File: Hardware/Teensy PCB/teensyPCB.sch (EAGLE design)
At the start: 13 parts, among them U1 HC_05, U2 USD-SOCKETNEW

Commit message: Added wiring of the Linear Array sensor to the teency chip
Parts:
- added LINEAR_ARRAY_SENSOR2: (no value), SparkFun-Connectors:M05LOCK
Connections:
- removed net N$3: J2.1
- removed net N$4: J1.1
- new net AOUT: LINEAR_ARRAY_SENSOR2.1, U$1.16/A2/T
- new net CLK: LINEAR_ARRAY_SENSOR2.3, U$1.14/A0
- new net SI: LINEAR_ARRAY_SENSOR2.2, U$1.15/A1/T
- net 3.3V: now also LINEAR_ARRAY_SENSOR2.4
- net GND: now also LINEAR_ARRAY_SENSOR2.5
- net N$5: now also J1.1

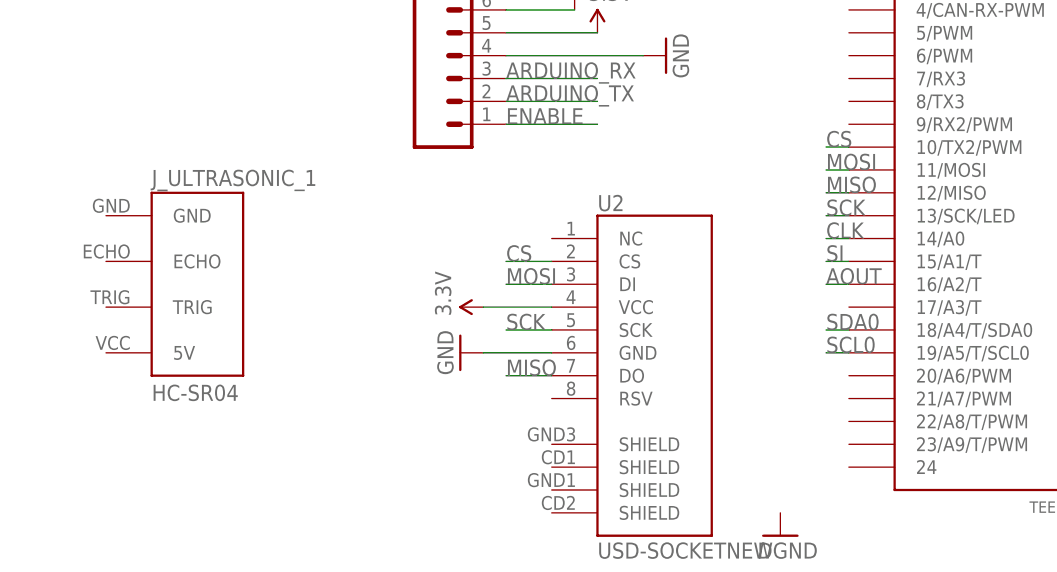
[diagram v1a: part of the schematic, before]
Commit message: Added the wiring for the ultrasonic sensor to the Teency chip
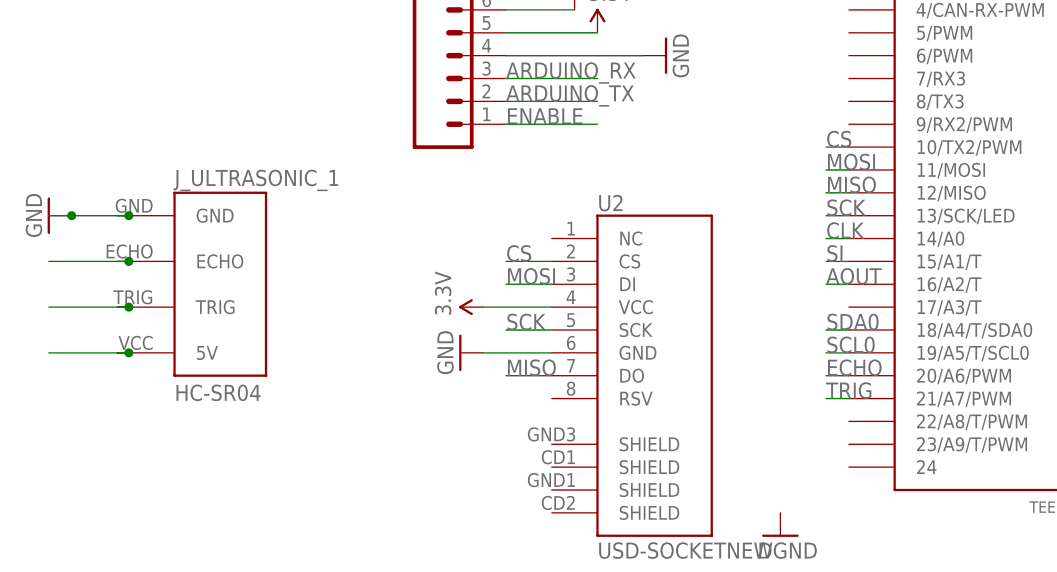
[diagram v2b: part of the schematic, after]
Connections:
- new net ECHO: J_ULTRASONIC_1.ECHO, U$1.20/A6/PWM
- new net TRIG: J_ULTRASONIC_1.TRIG, U$1.21/A7/PWM
- net 5V: now also J_ULTRASONIC_1.5V
- net GND: now also J_ULTRASONIC_1.GND
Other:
- moved on the sheet: J_ULTRASONIC_1
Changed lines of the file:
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@@
 <part name="GND7" library="SparkFun-Aesthetics" deviceset="GND" device=""/>
 <part name="SUPPLY8" library="SparkFun-Aesthetics" deviceset="3.3V" device=""/>
+<part name="GND8" library="SparkFun-Aesthetics" deviceset="GND" device=""/>
 </parts>
 <sheets>
@@
 <instance part="U1" gate="G$1" x="90.17" y="41.91"/>
 <instance part="J_BT_BOARD_1" gate="J_BT_BOARD" x="110.49" y="-1.27" rot="R180"/>
-<instance part="J_ULTRASONIC_1" gate="J_ULTRASONIC" x="-87.63" y="2.54"/>
+<instance part="J_ULTRASONIC_1" gate="J_ULTRASONIC" x="-85.09" y="2.54"/>
 <instance part="SUPPLY1" gate="G$1" x="35.56" y="40.64"/>
 <instance part="GND1" gate="1" x="30.48" y="33.02"/>
@@
 <instance part="GND7" gate="1" x="-71.12" y="60.96" rot="R90"/>
 <instance part="SUPPLY8" gate="G$1" x="-66.04" y="58.42"/>
+<instance part="GND8" gate="1" x="-106.68" y="10.16" rot="R270"/>
 </instances>
 <busses>
@@
 <pinref part="GND7" gate="1" pin="GND"/>
 </segment>
+<segment>
+<wire x1="-99.06" y1="10.16" x2="-97.79" y2="10.16" width="0.1524" layer="91"/>
+<pinref part="GND8" gate="1" pin="GND"/>
+<wire x1="-97.79" y1="10.16" x2="-104.14" y2="10.16" width="0.1524" layer="91"/>
+<wire x1="-104.14" y1="10.16" x2="-106.68" y2="10.16" width="0.1524" layer="91"/>
+<junction x="-104.14" y="10.16"/>
+<pinref part="J_ULTRASONIC_1" gate="J_ULTRASONIC" pin="GND"/>
+<junction x="-97.79" y="10.16"/>
+</segment>
 </net>
 <net name="3.3V" class="0">
@@
 <junction x="45.72" y="-10.16"/>
 <wire x1="45.72" y1="-10.16" x2="45.72" y2="-7.62" width="0.1524" layer="91"/>
+</segment>
+<segment>
+<wire x1="-99.06" y1="-5.08" x2="-97.79" y2="-5.08" width="0.1524" layer="91"/>
+<pinref part="J_ULTRASONIC_1" gate="J_ULTRASONIC" pin="5V"/>
+<wire x1="-97.79" y1="-5.08" x2="-106.68" y2="-5.08" width="0.1524" layer="91"/>
+<junction x="-97.79" y="-5.08"/>
 </segment>
 </net>
@@
 </segment>
 </net>
+<net name="ECHO" class="0">
+<segment>
+<wire x1="-99.06" y1="5.08" x2="-97.79" y2="5.08" width="0.1524" layer="91"/>
+<pinref part="J_ULTRASONIC_1" gate="J_ULTRASONIC" pin="ECHO"/>
+<wire x1="-97.79" y1="5.08" x2="-106.68" y2="5.08" width="0.1524" layer="91"/>
+<junction x="-97.79" y="5.08"/>
+</segment>
+<segment>
+<pinref part="U$1" gate="G$1" pin="20/A6/PWM"/>
+<wire x1="-17.78" y1="-7.62" x2="-20.32" y2="-7.62" width="0.1524" layer="91"/>
+<label x="-20.32" y="-7.62" size="1.778" layer="95"/>
+</segment>
+</net>
+<net name="TRIG" class="0">
+<segment>
+<wire x1="-99.06" y1="0" x2="-97.79" y2="0" width="0.1524" layer="91"/>
+<pinref part="J_ULTRASONIC_1" gate="J_ULTRASONIC" pin="TRIG"/>
+<wire x1="-97.79" y1="0" x2="-106.68" y2="0" width="0.1524" layer="91"/>
+<junction x="-97.79" y="0"/>
+</segment>
+<segment>
+<pinref part="U$1" gate="G$1" pin="21/A7/PWM"/>
+<wire x1="-17.78" y1="-10.16" x2="-20.32" y2="-10.16" width="0.1524" layer="91"/>
+<label x="-20.32" y="-10.16" size="1.778" layer="95"/>
+</segment>
+</net>

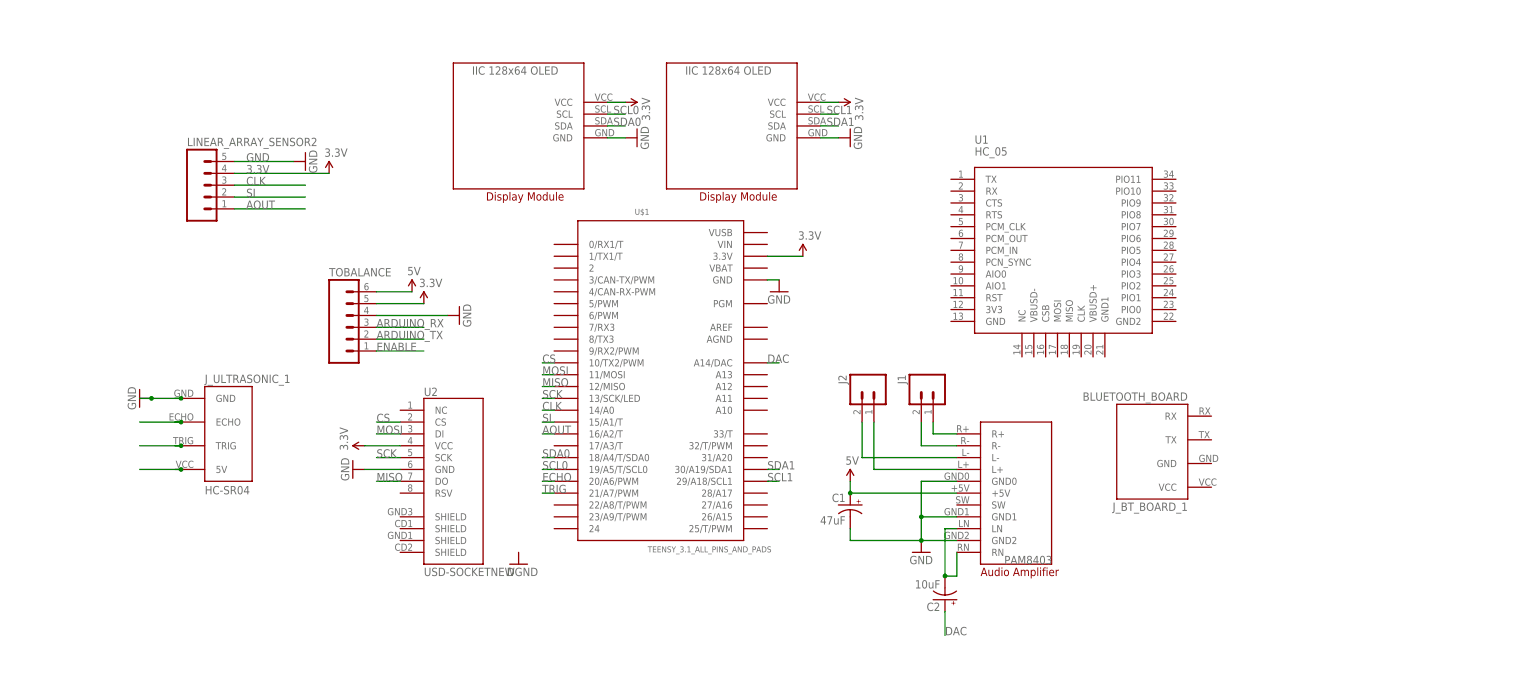
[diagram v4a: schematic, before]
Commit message: Abdul's changes. He did not save the .brd file so it will need to be regenerated
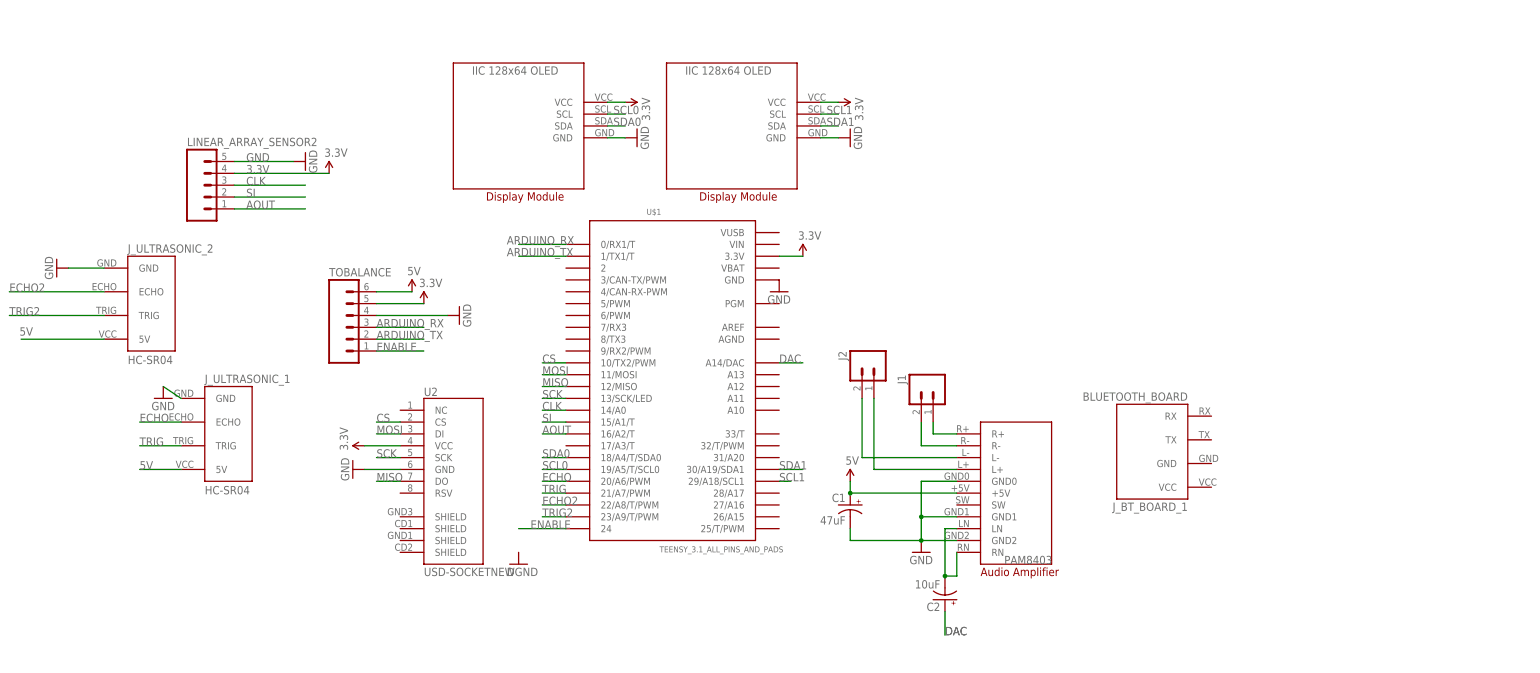
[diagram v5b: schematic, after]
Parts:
- removed U1: HC_05, Bluetooth_HC-05:HC_05
- added J_ULTRASONIC_2: HC-SR04, HC-SR04:HC-SR04
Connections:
- new net ECHO2: J_ULTRASONIC_2.ECHO, U$1.22/A8/T/PWM
- new net TRIG2: J_ULTRASONIC_2.TRIG, U$1.23/A9/T/PWM
- net 5V: now also J_ULTRASONIC_2.5V
- net ARDUINO_RX: now also U$1.0/RX1/T
- net ARDUINO_TX: now also U$1.1/TX1/T
- net ENABLE: now also U$1.24
- net GND: now also J_ULTRASONIC_2.GND
- net N$8: now also J2.1
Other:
- moved on the sheet: J2, U$1

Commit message: pcb update
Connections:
- net ENABLE: now also U$1.2; no longer U$1.24
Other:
- moved on the sheet: J_ULTRASONIC_1, J_ULTRASONIC_2, U$1

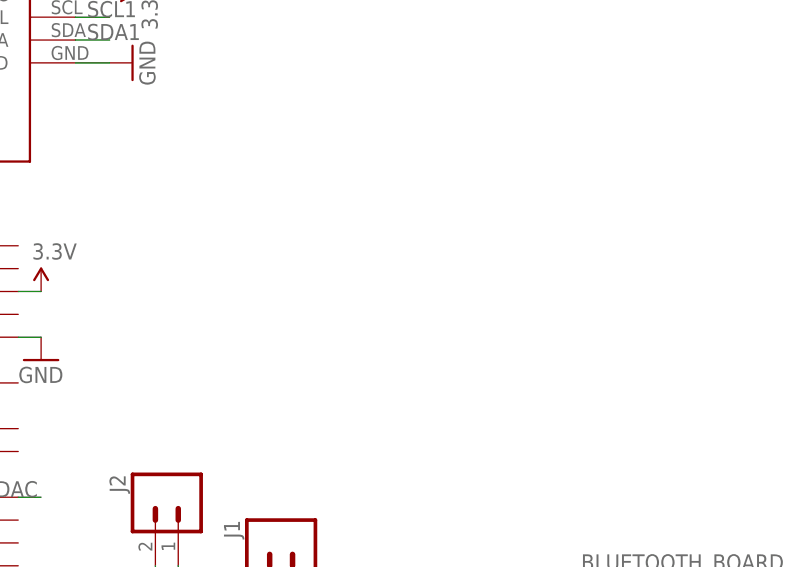
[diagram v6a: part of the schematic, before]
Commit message: Created library component for digipot
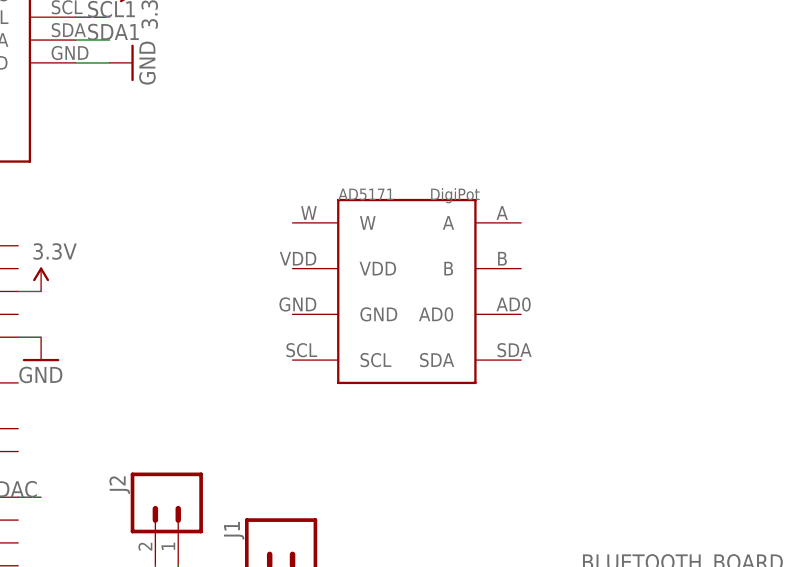
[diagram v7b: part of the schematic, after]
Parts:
- added U$5: DIGIPOT, DigiPot:DIGIPOT
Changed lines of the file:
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@@
 <?xml version="1.0" encoding="utf-8"?>
 <!DOCTYPE eagle SYSTEM "eagle.dtd">
-<eagle version="7.4.0">
+<eagle version="7.2.0">
 <drawing>
 <settings>
@@
 <part name="SUPPLY9" library="SparkFun-Aesthetics" deviceset="5V" device=""/>
 <part name="SUPPLY10" library="SparkFun-Aesthetics" deviceset="5V" device=""/>
+<part name="U$5" library="DigiPot" deviceset="DIGIPOT" device=""/>
 </parts>
 <sheets>
@@
 <instance part="SUPPLY9" gate="G$1" x="-106.68" y="-5.08"/>
 <instance part="SUPPLY10" gate="G$1" x="-124.46" y="22.86"/>
+<instance part="U$5" gate="G$1" x="76.2" y="40.64"/>
 </instances>
 <busses>

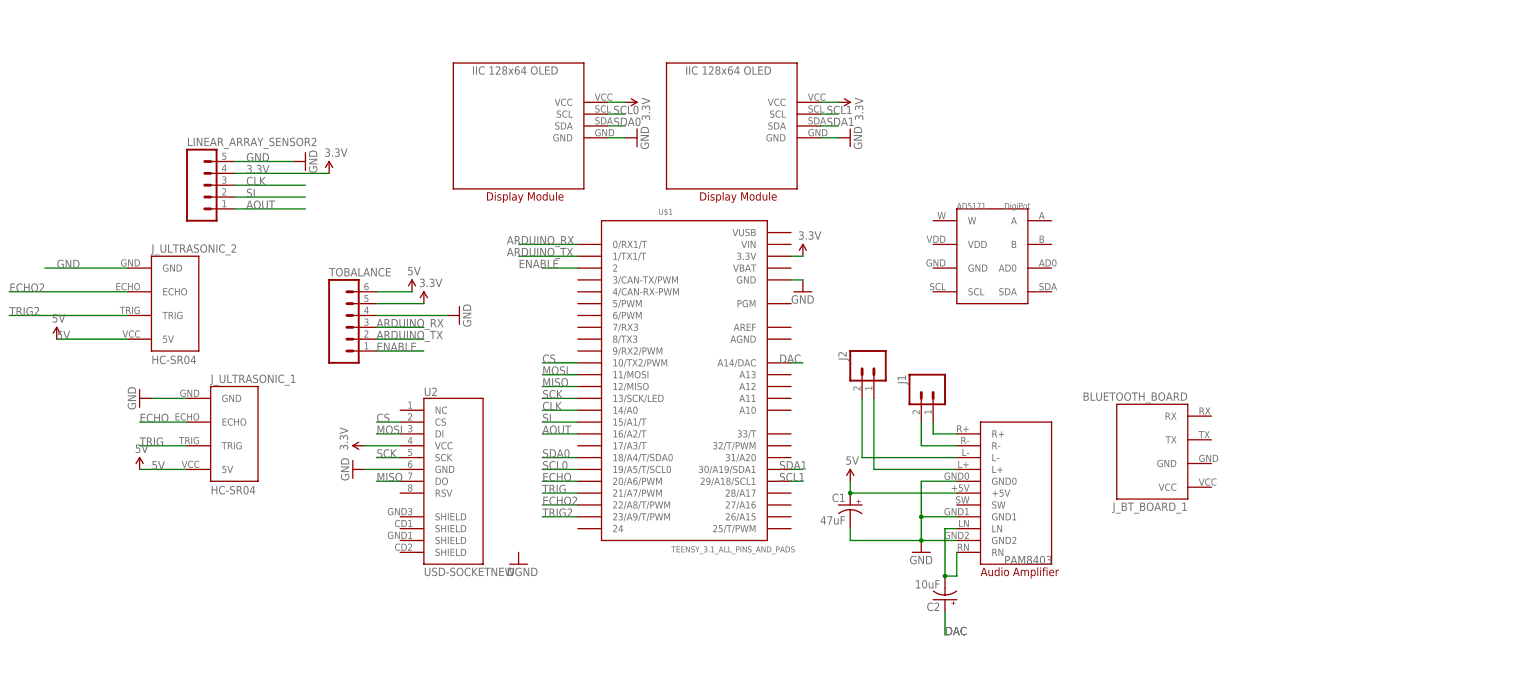
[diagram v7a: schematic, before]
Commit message: Wired digipot, added push buttons with voltage debounce, updated audio amplifier
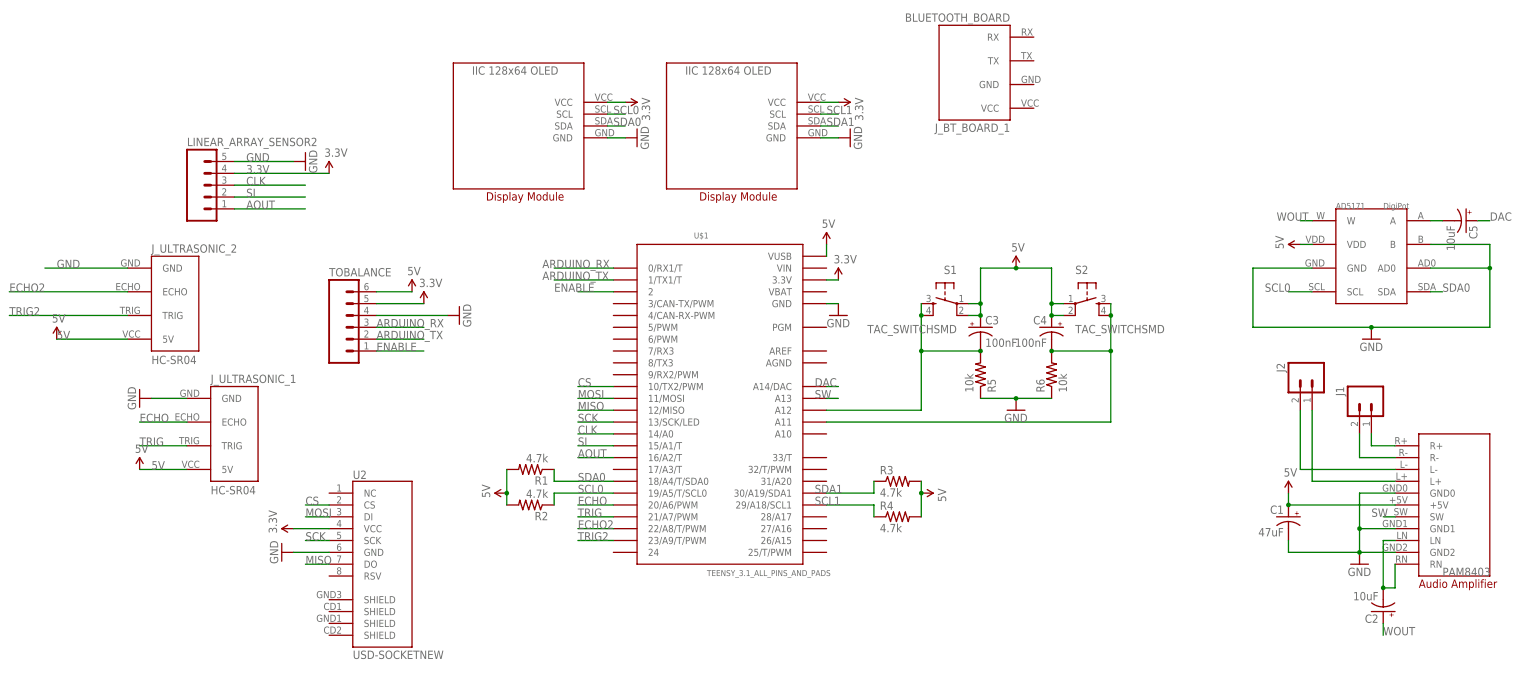
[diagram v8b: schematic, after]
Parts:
- added C3, C4: 100nF, SparkFun-Capacitors:CAP_POL3528
- added C5: 10uF, SparkFun-Capacitors:CAP_POL3528
- added R1, R2, R3, R4: 4.7k, SparkFun-Resistors:RESISTOR0805-RES
- added R5, R6: 10k, SparkFun-Resistors:RESISTOR0805-RES
- added S1, S2: TAC_SWITCHSMD, SparkFun-Retired:TAC_SWITCHSMD
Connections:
- new net N$2: C4.-, R6.2, S2.3, S2.4, U$1.A11
- new net N$3: C5.-, U$5.A
- new net N$9: C3.-, R5.2, S1.3, S1.4, U$1.A12
- new net SW: U$1.A13, U$4.SW
- new net WOUT: C2.+, U$5.W
- net 5V: now also C3.+, C4.+, R1.2, R2.2, R3.2, R4.2, S1.1, S1.2, S2.1, S2.2, U$1.VUSB, U$5.VDD
- net DAC: now also C5.+; no longer C2.+
- net GND: now also R5.1, R6.1, U$5.AD0, U$5.B, U$5.GND
- net SCL0: now also R2.1, U$5.SCL
- net SCL1: now also R4.1
- net SDA0: now also R1.1, U$5.SDA
- net SDA1: now also R3.1
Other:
- moved on the sheet: C1, C2, J1, J2, J_BT_BOARD_1, U$1, U2
